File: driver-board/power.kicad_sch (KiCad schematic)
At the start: 24 parts, among them J11 Conn_01x04, U2 LMR36510ADDA, U3 LMR36510ADDA

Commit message: schematic updates for r1
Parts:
- removed C17: 10uF 50V, Capacitor_SMD:C_1206_3216Metric, symbol Device:C_Small
- removed C18: .022uF 50V, Capacitor_SMD:C_1206_3216Metric, symbol Device:C_Small
- removed C21: 1uF, Capacitor_SMD:C_0805_2012Metric, symbol Device:C_Small
- removed C22: 0.1uF, Capacitor_SMD:C_0805_2012Metric, symbol Device:C_Small
- removed C23, C24, C25: 10uF, Capacitor_SMD:C_0805_2012Metric, symbol Device:C_Small
- removed L2: 47uH, footprints:SRN3010C2R2M, symbol Device:L
- removed R27: 100k, Resistor_SMD:R_0805_2012Metric, symbol Device:R_Small_US
- removed R28: 9.09k, Resistor_SMD:R_0805_2012Metric, symbol Device:R_Small_US
- removed U3: LMR36510ADDA, Package_SO:Texas_HTSOP-8-1EP_3.9x4.9mm_P1.27mm_EP2.95x4.9mm_Mask2.4x3.1mm_ThermalVias, symbol Regulator_Switching:LMR36510ADDA
- added J10: PJ-063AH, Connector_BarrelJack:BarrelJack_CUI_PJ-063AH_Horizontal, symbol Connector:Barrel_Jack_MountingPin
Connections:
- net V_FUSED is gone; now on net +12V: C10.1, C11.1, F1.2_1, U2.2 (VIN), U2.3 (EN)
- net GND: now also J10.2, J10.MP (MountPin)
- net at F1.1_1, J11.1 (Pin_1), J11.2 (Pin_2): now also J10.1

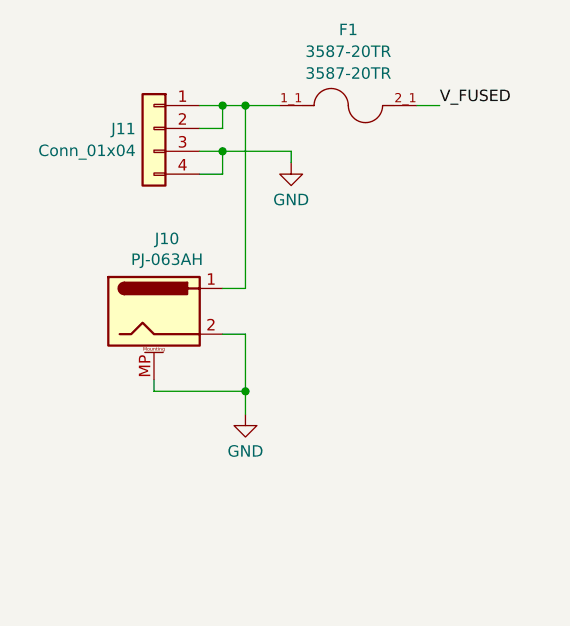
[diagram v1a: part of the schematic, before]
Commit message: updated layout
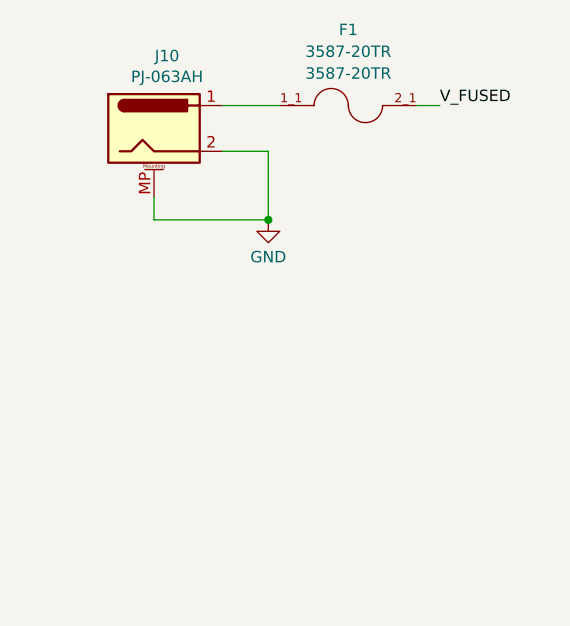
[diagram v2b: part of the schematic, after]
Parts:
- removed J11: Conn_01x04, footprints:CONN2_2601-3102_WAG, symbol Connector_Generic:Conn_01x04
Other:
- moved on the sheet: J10

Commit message: new board
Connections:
- net +12V: now also F1.2_2
- net at F1.1_1, J10.1: now also F1.1_2
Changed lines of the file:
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@@
+	)
+	(junction
+		(at 44.45 25.4)
+		(diameter 0)
+		(color 0 0 0 0)
 	)
 	(junction
@@
 	)
 	(junction
+		(at 62.23 25.4)
+		(diameter 0)
+		(color 0 0 0 0)
+	)
+	(junction
 		(at 201.93 58.42)
 		(diameter 0)
@@
 	(wire
 		(pts
+			(xy 44.45 25.4) (xy 45.72 25.4)
+		)
+		(stroke
+			(width 0)
+			(type default)
+		)
+	)
+	(wire
+		(pts
 			(xy 44.45 30.48) (xy 44.45 38.1)
 		)
@@
 	(wire
 		(pts
+			(xy 60.96 27.94) (xy 62.23 27.94)
+		)
+		(stroke
+			(width 0)
+			(type default)
+		)
+	)
+	(wire
+		(pts
 			(xy 102.87 101.6) (xy 110.49 101.6)
 		)
@@
 	(wire
 		(pts
+			(xy 62.23 27.94) (xy 62.23 25.4)
+		)
+		(stroke
+			(width 0)
+			(type default)
+		)
+	)
+	(wire
+		(pts
 			(xy 100.33 55.88) (xy 105.41 55.88)
 		)
@@
 	(wire
 		(pts
+			(xy 62.23 25.4) (xy 63.5 25.4)
+		)
+		(stroke
+			(width 0)
+			(type default)
+		)
+	)
+	(wire
+		(pts
 			(xy 180.34 58.42) (xy 172.72 58.42)
 		)
@@
 	(wire
 		(pts
+			(xy 44.45 27.94) (xy 44.45 25.4)
+		)
+		(stroke
+			(width 0)
+			(type default)
+		)
+	)
+	(wire
+		(pts
 			(xy 31.75 38.1) (xy 44.45 38.1)
 		)
@@
 	(wire
 		(pts
-			(xy 60.96 25.4) (xy 63.5 25.4)
+			(xy 60.96 25.4) (xy 62.23 25.4)
 		)
 		(stroke
@@
 	(wire
 		(pts
-			(xy 39.37 25.4) (xy 45.72 25.4)
+			(xy 39.37 25.4) (xy 44.45 25.4)
 		)
 		(stroke
@@
 		(pts
 			(xy 201.93 58.42) (xy 201.93 62.23)
+		)
+		(stroke
+			(width 0)
+			(type default)
+		)
+	)
+	(wire
+		(pts
+			(xy 45.72 27.94) (xy 44.45 27.94)
 		)
 		(stroke
@@
 			)
 		)
+		(pin "1_2"
+		)
 		(pin "1_1"
 		)
+		(pin "2_2"
+		)
 		(pin "2_1"
